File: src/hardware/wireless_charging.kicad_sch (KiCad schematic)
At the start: 25 parts

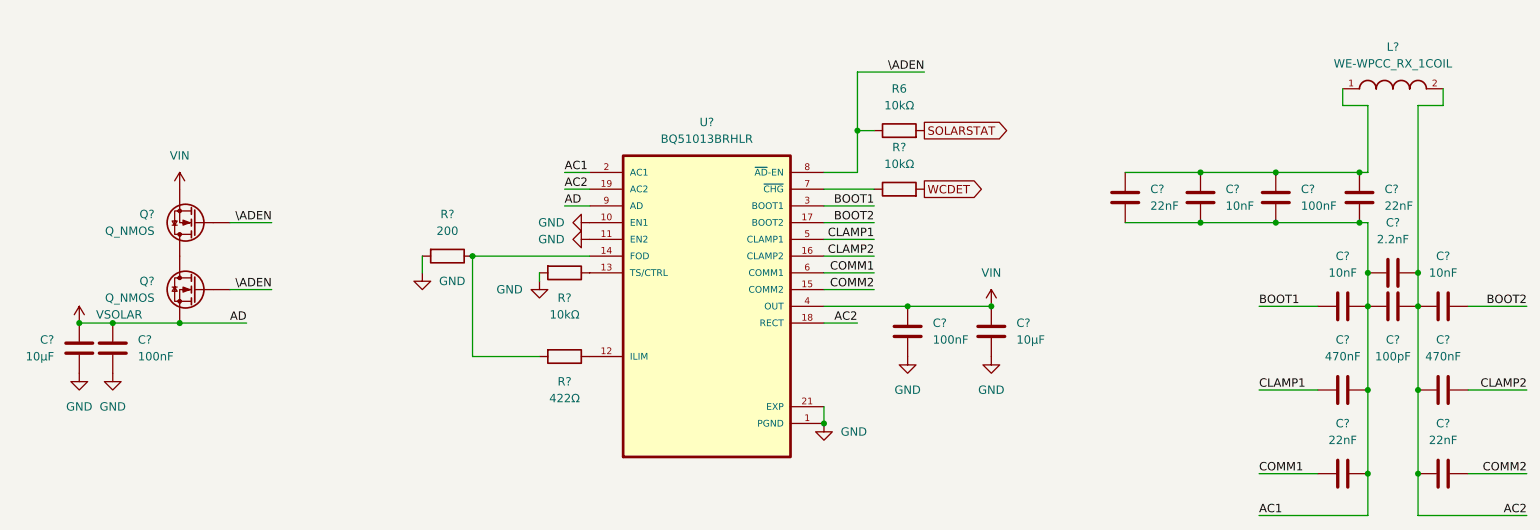
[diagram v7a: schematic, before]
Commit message: Cleanup & Fixes; Added footprints; Removed Light sensors
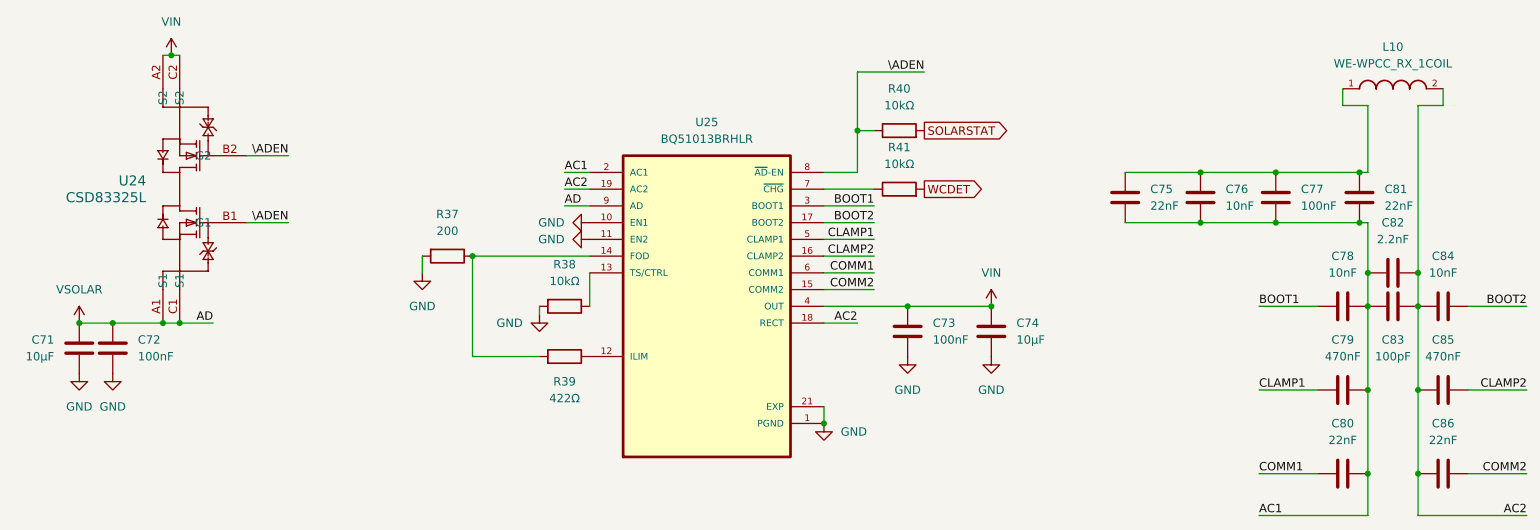
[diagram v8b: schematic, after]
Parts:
- removed Q? (x2): Q_NMOS, symbol Device:Q_NMOS
- added U24: CSD83325L, Project:YJE0006A, symbol CSD83325L:CSD83325L
- C71, C72, C73, C74, C75, C76, C77, C78, C79, C80, C81, C82, C83, C84, C85, C86: renamed from C?; footprint (none) -> Capacitor_SMD:C_0603_1608Metric
- L10: renamed from L?; footprint WE-WPCC_RX_1COIL:WE-WPCC_RX_760308103205 -> Project:WE-WPCC_RX_760308103205
- R37, R38, R39, R41: renamed from R?; footprint (none) -> Resistor_SMD:R_0603_1608Metric
- R40: renamed from R6; footprint (none) -> Resistor_SMD:R_0603_1608Metric
- U25: renamed from U?; footprint BQ51013BRHLR:IC_MSP430FR2522IRHLR -> Project:IC_MSP430FR2522IRHLR
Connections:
- net VIN: now also U24.A2 (S2), U24.C2 (S2)
- net VSOLAR: now also U24.A1 (S1), U24.C1 (S1)
- net \ADEN: now also U24.B1 (G1), U24.B2 (G2)
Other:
- moved on the sheet: R38
